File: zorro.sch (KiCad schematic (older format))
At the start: 43 parts, among them U1 SN74LVC8T245, U10 SN74LVC8T245, U11 SN74LVC8T245, U12 SN74LVC8T245, U13 SN74LVC8T245, U14 SN74LVC8T245, U15 SN74LVC8T245, U2 SN74LVC8T245, U3 74LVC2G07, U4 SN74LVC8T245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

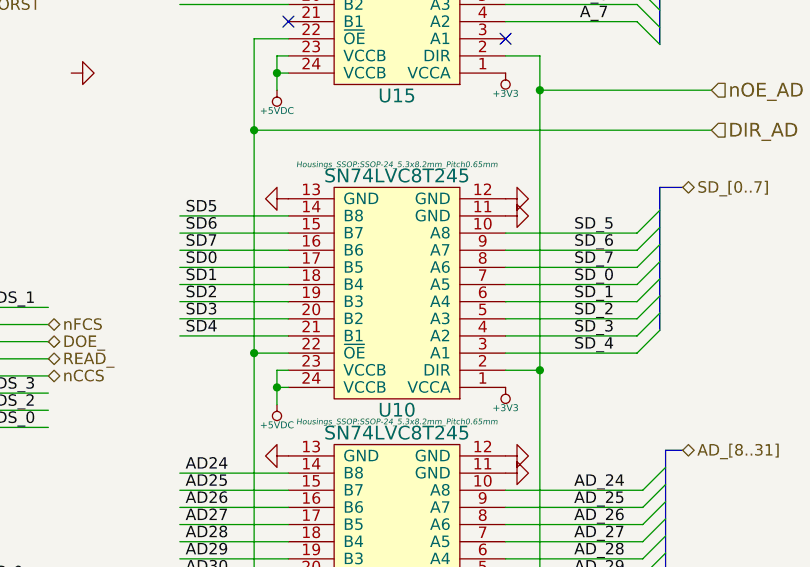
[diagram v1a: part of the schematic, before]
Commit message: SD lines rearranged
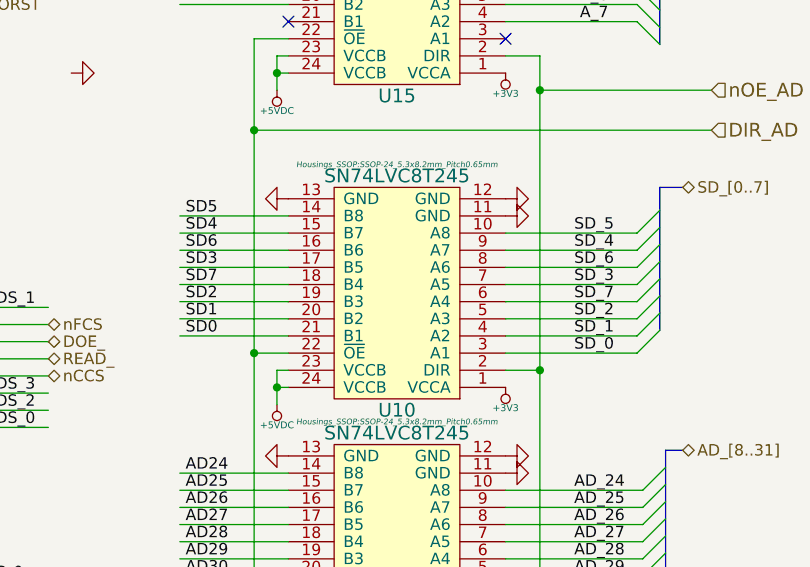
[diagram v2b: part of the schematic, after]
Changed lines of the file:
@@
 Text Label 13625 5450 0    50   ~ 0
 SD_5
+Text Label 13625 5600 0    50   ~ 0
+SD_6
+Text Label 13625 5750 0    50   ~ 0
+SD_7
 Text Label 13625 5525 0    50   ~ 0
-SD_6
-Text Label 13625 5600 0    50   ~ 0
-SD_7
-Text Label 13625 5975 0    50   ~ 0
 SD_4
-Text Label 13625 5900 0    50   ~ 0
+Text Label 13625 5675 0    50   ~ 0
 SD_3
 Text Label 13625 5825 0    50   ~ 0
 SD_2
-Text Label 13625 5750 0    50   ~ 0
+Text Label 13625 5900 0    50   ~ 0
 SD_1
-Text Label 13625 5675 0    50   ~ 0
+Text Label 13625 5975 0    50   ~ 0
 SD_0
 Text HLabel 14100 5250 2    50   BiDi ~ 0
@@
 Text Label 11925 5375 0    50   ~ 0
 SD5
+Text Label 11925 5525 0    50   ~ 0
+SD6
+Text Label 11925 5675 0    50   ~ 0
+SD7
 Text Label 11925 5450 0    50   ~ 0
-SD6
-Text Label 11925 5525 0    50   ~ 0
-SD7
-Text Label 11925 5900 0    50   ~ 0
 SD4
-Text Label 11925 5825 0    50   ~ 0
+Text Label 11925 5600 0    50   ~ 0
 SD3
 Text Label 11925 5750 0    50   ~ 0
 SD2
-Text Label 11925 5675 0    50   ~ 0
+Text Label 11925 5825 0    50   ~ 0
 SD1
-Text Label 11925 5600 0    50   ~ 0
+Text Label 11925 5900 0    50   ~ 0
 SD0
 $Comp

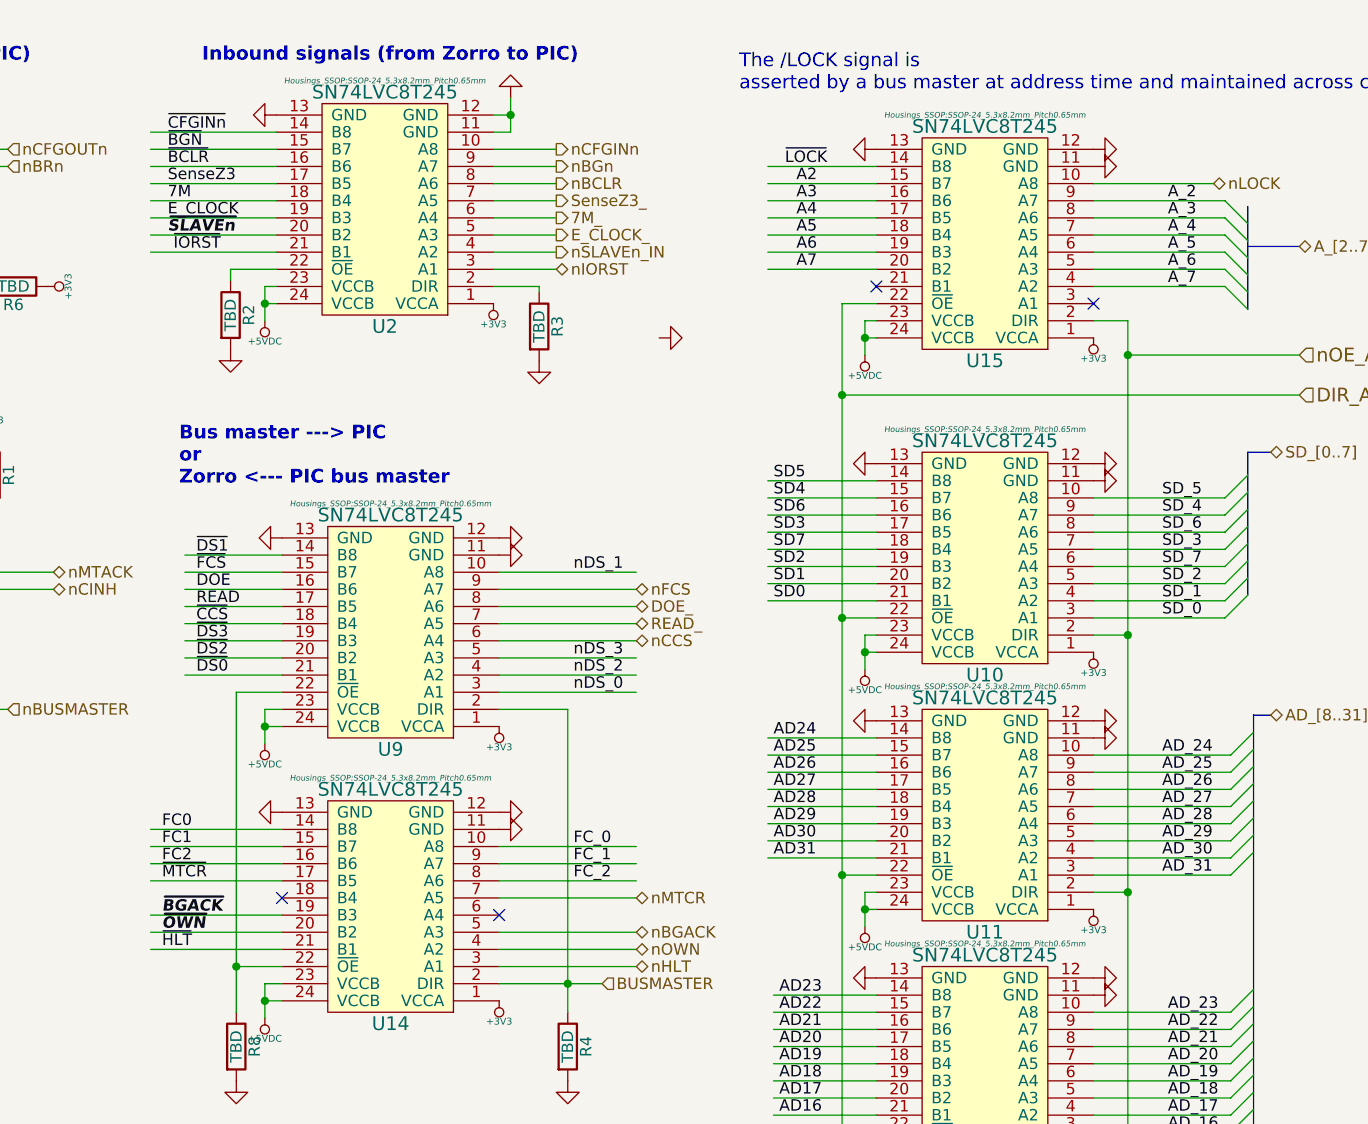
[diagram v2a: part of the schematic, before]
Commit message: More 5V signals rearranged
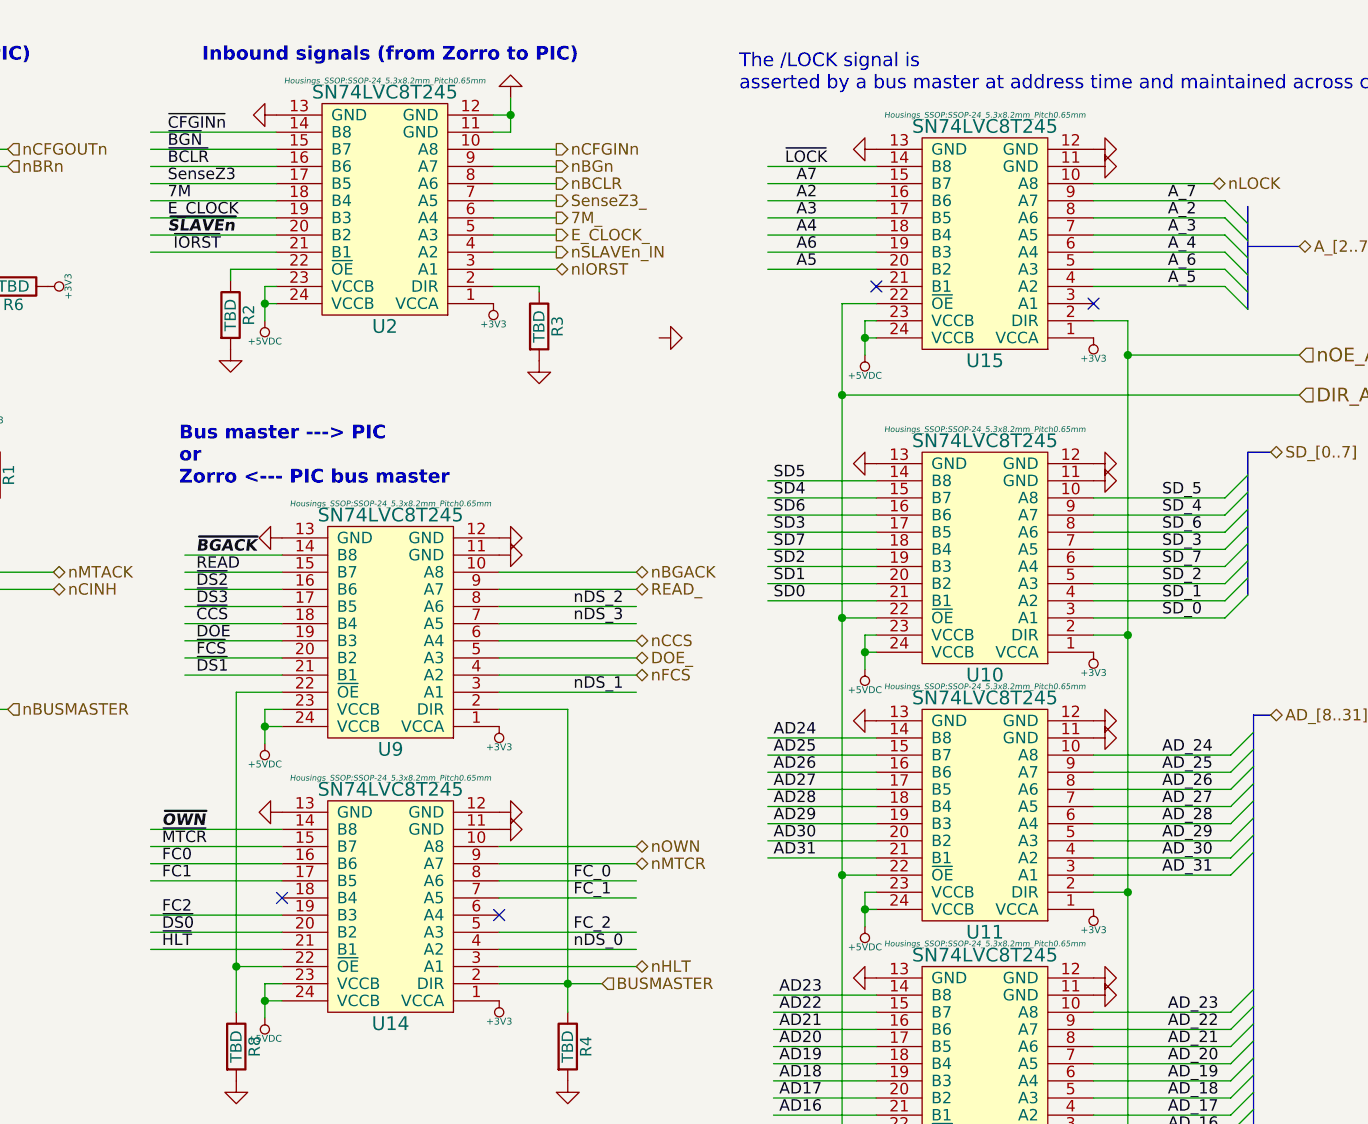
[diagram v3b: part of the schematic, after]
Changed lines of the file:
@@
 Text Label 2950 2425 0    50   ~ 0
 ~CCS
-Text HLabel 11325 5850 2    50   BiDi ~ 0
+Text HLabel 11325 6225 2    50   BiDi ~ 0
 nFCS
 Text HLabel 11325 6075 2    50   BiDi ~ 0
 nCCS
-Text HLabel 11325 5925 2    50   BiDi ~ 0
+Text HLabel 11325 6150 2    50   BiDi ~ 0
 DOE_
 Entry Wire Line
@@
 Text Label 2950 2650 0    50   ~ 0
 READ
-Text HLabel 11325 6000 2    50   BiDi ~ 0
+Text HLabel 11325 5850 2    50   BiDi ~ 0
 READ_
 Text Label 2950 1675 0    50   ~ 0
@@
 Text HLabel 8775 5775 2    50   BiDi ~ 0
 nMTACK
-Text HLabel 11325 7200 2    50   BiDi ~ 0
+Text HLabel 11325 7050 2    50   BiDi ~ 0
 nMTCR
 Text HLabel 14225 4350 2    50   BiDi ~ 0
@@
 Text HLabel 7175 8225 2    50   Input ~ 0
 nSLAVEn_OUT
-Text Label 9400 5700 0    50   ~ 0
+Text Label 9400 6225 0    50   ~ 0
 ~DS1
-Text Label 9400 5775 0    50   ~ 0
+Text Label 9400 6150 0    50   ~ 0
 ~FCS
 Text Label 9275 4000 0    50   ~ 0
 ~BCLR
-Text Label 9400 5850 0    50   ~ 0
+Text Label 9400 6075 0    50   ~ 0
 DOE
 Text Label 9300 4375 0    50   ~ 0
@@
 Text Label 9400 6000 0    50   ~ 0
 ~CCS
-Text Label 9400 6075 0    50   ~ 0
+Text Label 9400 5925 0    50   ~ 0
 ~DS3
-Text Label 9400 6150 0    50   ~ 0
+Text Label 9400 5850 0    50   ~ 0
 ~DS2
-Text Label 9400 5925 0    50   ~ 0
+Text Label 9400 5775 0    50   ~ 0
 READ
 $Comp
@@
 Text Label 11950 9275 0    50   ~ 0
 AD8
-Text Label 9400 6225 0    50   ~ 0
+Text Label 9250 7350 0    50   ~ 0
 ~DS0
+Text Label 9250 7275 0    50   ~ 0
+FC2
+Text Label 9250 7125 0    50   ~ 0
+FC1
 Text Label 9250 7050 0    50   ~ 0
-FC2
-Text Label 9250 6975 0    50   ~ 0
-FC1
-Text Label 9250 6900 0    50   ~ 0
 FC0
 Text Label 6925 5700 0    50   ~ 0
 ~MTACK
-Text Label 9250 7125 0    50   ~ 0
+Text Label 9250 6975 0    50   ~ 0
 ~MTCR
 $Comp
@@
 Text Label 11975 4000 0    50   ~ 0
 ~LOCK
-Text Label 11050 5775 0    50   ~ 0
+Text Label 11050 6300 0    50   ~ 0
 nDS_1
-Text Label 11050 6150 0    50   ~ 0
+Text Label 11050 6000 0    50   ~ 0
 nDS_3
-Text Label 11050 6225 0    50   ~ 0
+Text Label 11050 5925 0    50   ~ 0
 nDS_2
-Text Label 11050 6300 0    50   ~ 0
+Text Label 11050 7425 0    50   ~ 0
 nDS_0
+Text Label 11050 7350 0    50   ~ 0
+FC_2
+Text Label 11050 7200 0    50   ~ 0
+FC_1
 Text Label 11050 7125 0    50   ~ 0
-FC_2
-Text Label 11050 7050 0    50   ~ 0
-FC_1
-Text Label 11050 6975 0    50   ~ 0
 FC_0
-Text Label 12025 4075 0    50   ~ 0
+Text Label 12025 4150 0    50   ~ 0
 A2
-Text Label 12025 4150 0    50   ~ 0
+Text Label 12025 4225 0    50   ~ 0
 A3
-Text Label 12025 4225 0    50   ~ 0
+Text Label 12025 4300 0    50   ~ 0
 A4
-Text Label 12025 4300 0    50   ~ 0
+Text Label 12025 4450 0    50   ~ 0
 A5
 Text Label 12025 4375 0    50   ~ 0
 A6
-Text Label 12025 4450 0    50   ~ 0
+Text Label 12025 4075 0    50   ~ 0
 A7
 $Comp
@@
 	-1   0    0    1
 $EndComp
-Text Label 13650 4150 0    50   ~ 0
+Text Label 13650 4225 0    50   ~ 0
 A_2
-Text Label 13650 4225 0    50   ~ 0
+Text Label 13650 4300 0    50   ~ 0
 A_3
-Text Label 13650 4300 0    50   ~ 0
+Text Label 13650 4375 0    50   ~ 0
 A_4
-Text Label 13650 4375 0    50   ~ 0
+Text Label 13650 4525 0    50   ~ 0
 A_5
 Text Label 13650 4450 0    50   ~ 0
 A_6
-Text Label 13650 4525 0    50   ~ 0
+Text Label 13650 4150 0    50   ~ 0
 A_7
 $Comp
@@
 Text Notes 9425 3550 0    60   ~ 12
 Inbound signals (from Zorro to PIC)
-Text Label 9250 7275 0    50   Italic 10
+Text Label 9400 5700 0    50   Italic 10
 ~BGACK
-Text Label 9250 7350 0    50   Italic 10
+Text Label 9250 6900 0    50   Italic 10
 ~OWN
 Text Label 9275 4225 0    50   ~ 0
@@
 Wire Wire Line
 	10725 7425 11325 7425
-Text HLabel 11325 7350 2    50   BiDi ~ 0
+Text HLabel 11325 5775 2    50   BiDi ~ 0
 nBGACK
-Text HLabel 11325 7425 2    50   BiDi ~ 0
+Text HLabel 11325 6975 2    50   BiDi ~ 0
 nOWN
 $Comp

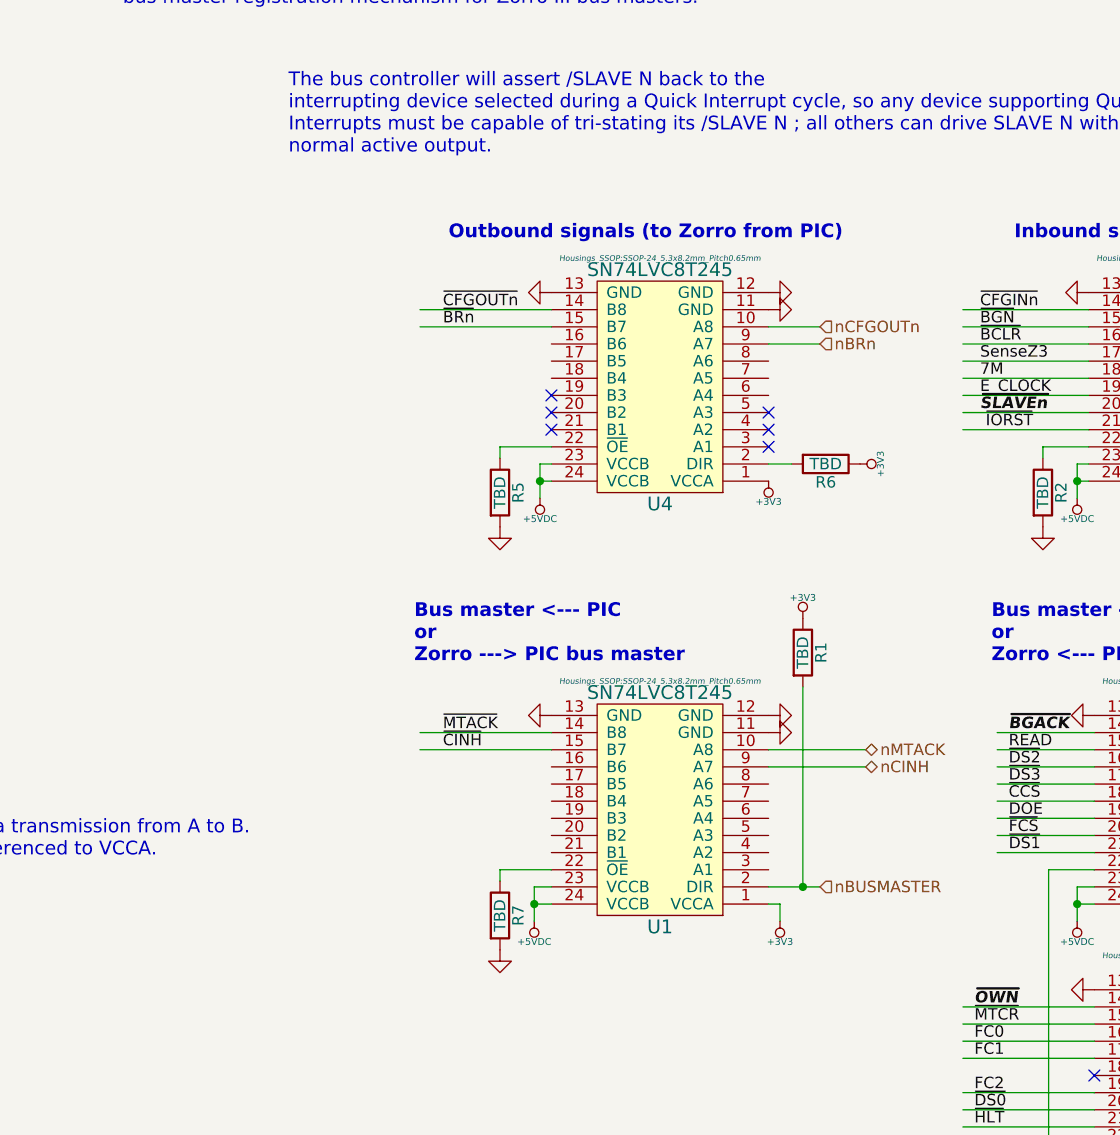
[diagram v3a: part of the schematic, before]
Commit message: Add SN74LVC2T45
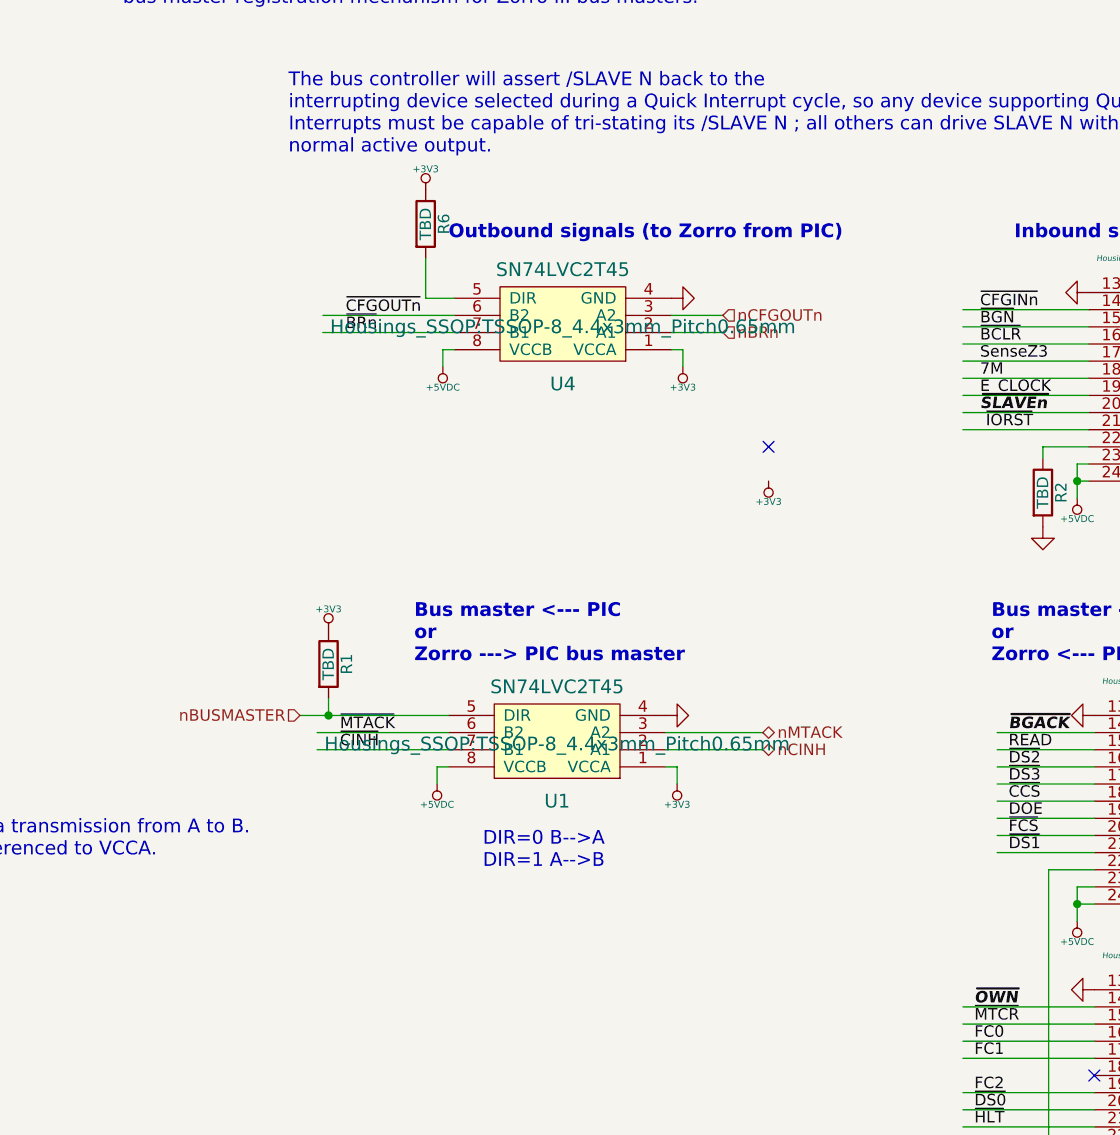
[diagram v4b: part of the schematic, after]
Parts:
- removed R5, R7: TBD, Resistors_SMD:R_0603, symbol R
- removed U1, U4: SN74LVC8T245, Housings_SSOP:SSOP-24_5.3x8.2mm_Pitch0.65mm, symbol SN74LVC8T245
- added U1, U4: SN74LVC2T45, Housings_SSOP:TSSOP-8_4.4x3mm_Pitch0.65mm, symbol SN74LVC2T45
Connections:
- wire segments 296 -> 293
- no-connect marks 14 -> 9
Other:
- note added: "DIR=0 B-->A\nDIR=1 A-->B"
- moved on the sheet: R1, R6

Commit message: Massive board changes
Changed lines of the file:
@@
-	0    -1   -1   0
-$EndComp
-$Comp
-L GND #PWR029
-U 1 1 57F603C9
-P 11425 4750
-F 0 "#PWR029" H 11425 4500 50  0001 C CNN
-F 1 "GND" H 11425 4600 50  0001 C CNN
-F 2 "" H 11425 4750 50  0000 C CNN
-F 3 "" H 11425 4750 50  0000 C CNN
-	1    11425 4750
 	0    -1   -1   0
 $EndComp
@@
 F 0 "U1" H 7425 6000 60  0000 C CNN
 F 1 "SN74LVC2T45" H 7425 5500 60  0000 C CNN
-F 2 "Housings_SSOP:TSSOP-8_4.4x3mm_Pitch0.65mm" H 7425 5750 60  0000 C CNN
+F 2 "Housings_SSOP:TSSOP-8_4.4x3mm_Pitch0.65mm" H 7425 5925 25  0000 C CIB
 F 3 "" H 7425 5750 60  0001 C CNN
 	1    7425 5750
@@
 F 0 "U4" H 7450 4175 60  0000 C CNN
 F 1 "SN74LVC2T45" H 7450 3675 60  0000 C CNN
-F 2 "Housings_SSOP:TSSOP-8_4.4x3mm_Pitch0.65mm" H 7450 3925 60  0000 C CNN
+F 2 "Housings_SSOP:TSSOP-8_4.4x3mm_Pitch0.65mm" H 7450 4100 25  0000 C CIB
 F 3 "" H 7450 3925 60  0001 C CNN
 	1    7450 3925

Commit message: Moar
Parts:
- removed R2, R3: TBD, Resistors_SMD:R_0603, symbol R
- removed U2: SN74LVC8T245, Housings_SSOP:SSOP-24_5.3x8.2mm_Pitch0.65mm, symbol SN74LVC8T245
- added C57, C58, C59, C60: 0,1, Capacitors_SMD:C_0603, symbol C
- added U16, U17, U18, U2: SN74LVC2T45, Housings_SSOP:TSSOP-8_3x3mm_Pitch0.65mm, symbol SN74LVC2T45
- U1, U4: footprint Housings_SSOP:TSSOP-8_4.4x3mm_Pitch0.65mm -> Housings_SSOP:TSSOP-8_3x3mm_Pitch0.65mm
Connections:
- wire segments 293 -> 283
- no-connect marks 9 -> 8
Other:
- moved on the sheet: C18, C19, C20, C21, C22, C23, C24, C25, C26, C27, C28, C29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

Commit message: PCB updates
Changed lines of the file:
@@
 Text HLabel 8150 3875 2    50   Input ~ 0
 nBRn
-Text HLabel 10875 4800 2    50   Output ~ 0
+Text HLabel 10875 4725 2    50   Output ~ 0
 nBGn
 Text HLabel 10875 3850 2    50   Output ~ 0
@@
 Text Label 9250 7425 0    50   Italic 10
 ~OWN
-Text Label 9200 4725 0    50   ~ 0
+Text Label 9225 4800 0    50   ~ 0
 E_CLOCK
 Text HLabel 14225 5000 2    60   Input ~ 0
@@
 Text HLabel 10875 3775 2    50   Output ~ 0
 7M_
-Text HLabel 10875 4725 2    50   Output ~ 0
+Text HLabel 10875 4800 2    50   Output ~ 0
 E_CLOCK_
 Wire Wire Line
@@
 Text Label 9200 4250 0    50   ~ 0
 ~CFGINn
-Text Label 9200 4800 0    50   ~ 0
+Text Label 9225 4725 0    50   ~ 0
 ~BGN
 $Comp
